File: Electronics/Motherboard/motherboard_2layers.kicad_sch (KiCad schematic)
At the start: 55 parts, among them J1 DX07S024JJ3R1300, J2 Conn_02x10_Odd_Even, M1 AO3400A, M2 AO3400A, M3 AO3400A, U1 AMS1117-3.3, U2 TMC2209_SILENTSTEPSTICK, U3 TMC2209_SILENTSTEPSTICK, U4 TMC2209_SILENTSTEPSTICK, U5 TMC2209_SILENTSTEPSTICK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

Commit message: yay finished
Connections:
- net DIAG_M3: now also U7.96 (PE2); no longer U7.2 (PC10)
- net DIR_M4: now also U7.76 (PC8); no longer U7.72 (PF8)
- net EN_BTN: now also U7.21 (PC0); no longer U7.44 (PE11)
- net EN_FOR: now also U7.23 (PC2); no longer U7.46 (PE13)
- net EN_M1: now also U7.78 (PD0); no longer U7.68 (PD15)
- net EN_REV: now also U7.22 (PC1); no longer U7.45 (PE12)
- net STEP_M1: now also U7.79 (PD1); no longer U7.67 (PD14)
- net STEP_M2: now also U7.97 (PE3); no longer U7.33 (PC4)
- net STEP_M3: now also U7.95 (PE1); no longer U7.3 (PC11)
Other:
- note added: "Voltage Reg 3.3v"
- note added: "Voltage Reg. 5v"
- note removed: "Voltage Regulator"
- moved on the sheet: C8, C9, U6

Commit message: updated some files
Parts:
- added U8: STM32F405RGTx, Package_QFP:LQFP-64_10x10mm_P0.5mm, symbol MCU_ST_STM32F4:STM32F405RGTx
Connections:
- net STEP_M2: now also U7.33 (PC4); no longer U7.97 (PE3)
- net STEP_M4: now also U7.97 (PE3); no longer U7.1 (PB9)
- new net: U8.18 (VSS), U8.63 (VSS)
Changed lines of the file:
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@@
 		(color 0 0 0 0)
 	)
+	(bus_entry
+		(at 103.124 97.028)
+		(size 2.54 2.54)
+		(stroke
+			(width 0)
+			(type default)
+		)
+	)
+	(bus_entry
+		(at 79.248 41.402)
+		(size 2.54 2.54)
+		(stroke
+			(width 0)
+			(type default)
+		)
+	)
 	(wire
 		(pts
@@
 		)
 	)
+	(global_label "STEP_M4"
+		(shape input)
+		(at 39.37 132.08 180)
+		(fields_autoplaced yes)
+		(effects
+			(font
+				(size 1.27 1.27)
+			)
+			(justify right)
+		)
+		(property "Intersheetrefs" "${INTERSHEET_REFS}"
+			(at 28.1602 132.08 0)
+			(effects
+				(font
+					(size 1.27 1.27)
+				)
+				(justify right)
+				(hide yes)
+			)
+		)
+	)
 	(global_label "ABL"
 		(shape input)
@@
 		)
 	)
-	(global_label "STEP_M4"
-		(shape input)
-		(at 85.09 147.32 0)
-		(fields_autoplaced yes)
-		(effects
-			(font
-				(size 1.27 1.27)
-			)
-			(justify left)
-		)
-		(property "Intersheetrefs" "${INTERSHEET_REFS}"
-			(at 96.2998 147.32 0)
-			(effects
-				(font
-					(size 1.27 1.27)
-				)
-				(justify left)
-				(hide yes)
-			)
-		)
-	)
 	(global_label "UART_TX"
 		(shape input)
@@
 		)
 	)
-	(global_label "STEP_M2"
-		(shape input)
-		(at 39.37 132.08 180)
-		(fields_autoplaced yes)
-		(effects
-			(font
-				(size 1.27 1.27)
-			)
-			(justify right)
-		)
-		(property "Intersheetrefs" "${INTERSHEET_REFS}"
-			(at 28.1602 132.08 0)
-			(effects
-				(font
-					(size 1.27 1.27)
-				)
-				(justify right)
-				(hide yes)
-			)
-		)
-	)
 	(global_label "EN_M3"
 		(shape input)
@@
 		)
 	)
+	(global_label "STEP_M2"
+		(shape input)
+		(at 85.09 177.8 0)
+		(fields_autoplaced yes)
+		(effects
+			(font
+				(size 1.27 1.27)
+			)
+			(justify left)
+		)
+		(property "Intersheetrefs" "${INTERSHEET_REFS}"
+			(at 96.2998 177.8 0)
+			(effects
+				(font
+					(size 1.27 1.27)
+				)
+				(justify left)
+				(hide yes)
+			)
+		)
+	)
 	(global_label "UART_TX"
 		(shape input)
@@
 					(unit 1)
 				)
+			)
+		)
+	)
+	(symbol
+		(lib_id "MCU_ST_STM32F4:STM32F405RGTx")
+		(at 119.888 122.428 0)
+		(unit 1)
+		(exclude_from_sim no)
+		(in_bom yes)
+		(on_board yes)
+		(dnp no)
+		(fields_autoplaced yes)
+		(property "Reference" "U8"
+			(at 124.6221 167.64 0)
+			(effects
+				(font
+					(size 1.27 1.27)
+				)
+				(justify left)
+			)
+		)
+		(property "Value" "STM32F405RGTx"
+			(at 124.6221 170.18 0)
+			(effects
+				(font
+					(size 1.27 1.27)
+				)
+				(justify left)
+			)
+		)
+		(property "Footprint" "Package_QFP:LQFP-64_10x10mm_P0.5mm"
+			(at 104.648 165.608 0)
+			(effects
+				(font
+					(size 1.27 1.27)
+				)
+				(justify right)
+				(hide yes)
+			)
+		)
+		(property "Datasheet" "https://www.st.com/resource/en/datasheet/stm32f405rg.pdf"
+			(at 119.888 122.428 0)
+			(effects
+				(font
+					(size 1.27 1.27)
+				)
+				(hide yes)
+			)
+		)
+		(property "Description" "STMicroelectronics Arm Cortex-M4 MCU, 1024KB flash, 192KB RAM, 168 MHz, 1.8-3.6V, 51 GPIO, LQFP64"
+			(at 119.888 122.428 0)
+			(effects
+				(font
+					(size 1.27 1.27)
+				)
+				(hide yes)
+			)
+		)
+		(pin "63"
+		)
+		(pin "7"
+		)
+		(pin "50"
+		)
+		(pin "31"
+		)
+		(pin "33"
+		)
+		(pin "12"
+		)
+		(pin "34"
+		)
+		(pin "39"
+		)
+		(pin "44"
+		)
+		(pin "46"
+		)
+		(pin "60"
+		)
+		(pin "20"
+		)
+		(pin "36"
+		)
+		(pin "55"
+		)
+		(pin "15"
+		)
+		(pin "18"
+		)
+		(pin "37"
+		)
+		(pin "58"
+		)
+		(pin "2"
+		)
+		(pin "47"
+		)
+		(pin "5"
+		)
+		(pin "54"
+		)
+		(pin "62"
+		)
+		(pin "13"
+		)
+		(pin "53"
+		)
+		(pin "56"
+		)
+		(pin "27"
+		)
+		(pin "42"
+		)
+		(pin "59"
+		)
+		(pin "40"
+		)
+		(pin "64"
+		)
+		(pin "19"
+		)
+		(pin "48"
+		)
+		(pin "23"
+		)
+		(pin "32"
+		)
+		(pin "22"
+		)
+		(pin "41"
+		)
+		(pin "17"
+		)
+		(pin "49"
+		)
+		(pin "30"
+		)
+		(pin "10"
+		)
+		(pin "51"
+		)
+		(pin "43"
+		)
+		(pin "57"
+		)
+		(pin "6"
+		)
+		(pin "61"
+		)
+		(pin "26"
+		)
+		(pin "1"
+		)
+		(pin "11"
+		)
+		(pin "14"
+		)
+		(pin "16"
+		)
+		(pin "21"
+		)
+		(pin "25"
+		)
+		(pin "28"
+		)
+		(pin "29"
+		)
+		(pin "3"
+		)
+		(pin "38"
+		)
+		(pin "4"
+		)
+		(pin "45"
+		)
+		(pin "52"
+		)
+		(pin "35"
+		)
+		(pin "24"
+		)
+		(pin "9"
+		)
+		(pin "8"
+		)
+		(instances
+			(project ""
+				(path "/9290e430-09f5-4a3f-8744-4071dceedc2e"
+					(reference "U8")
+					(unit 1)
+				)

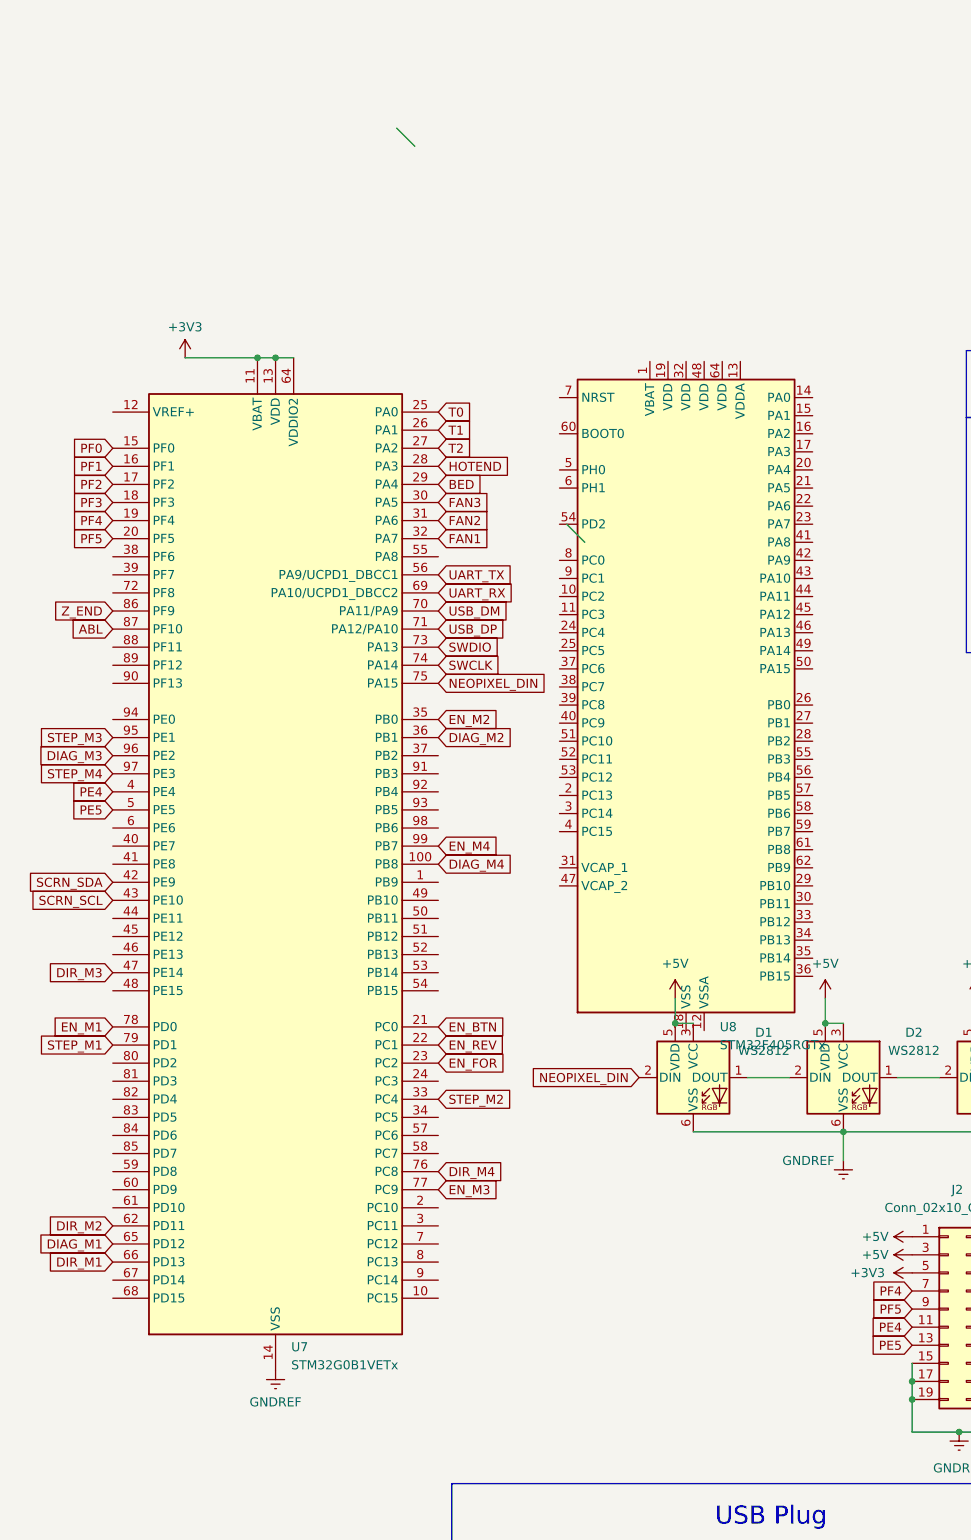
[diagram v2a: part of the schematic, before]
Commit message: updating the sch to work ebtter with the new mcu
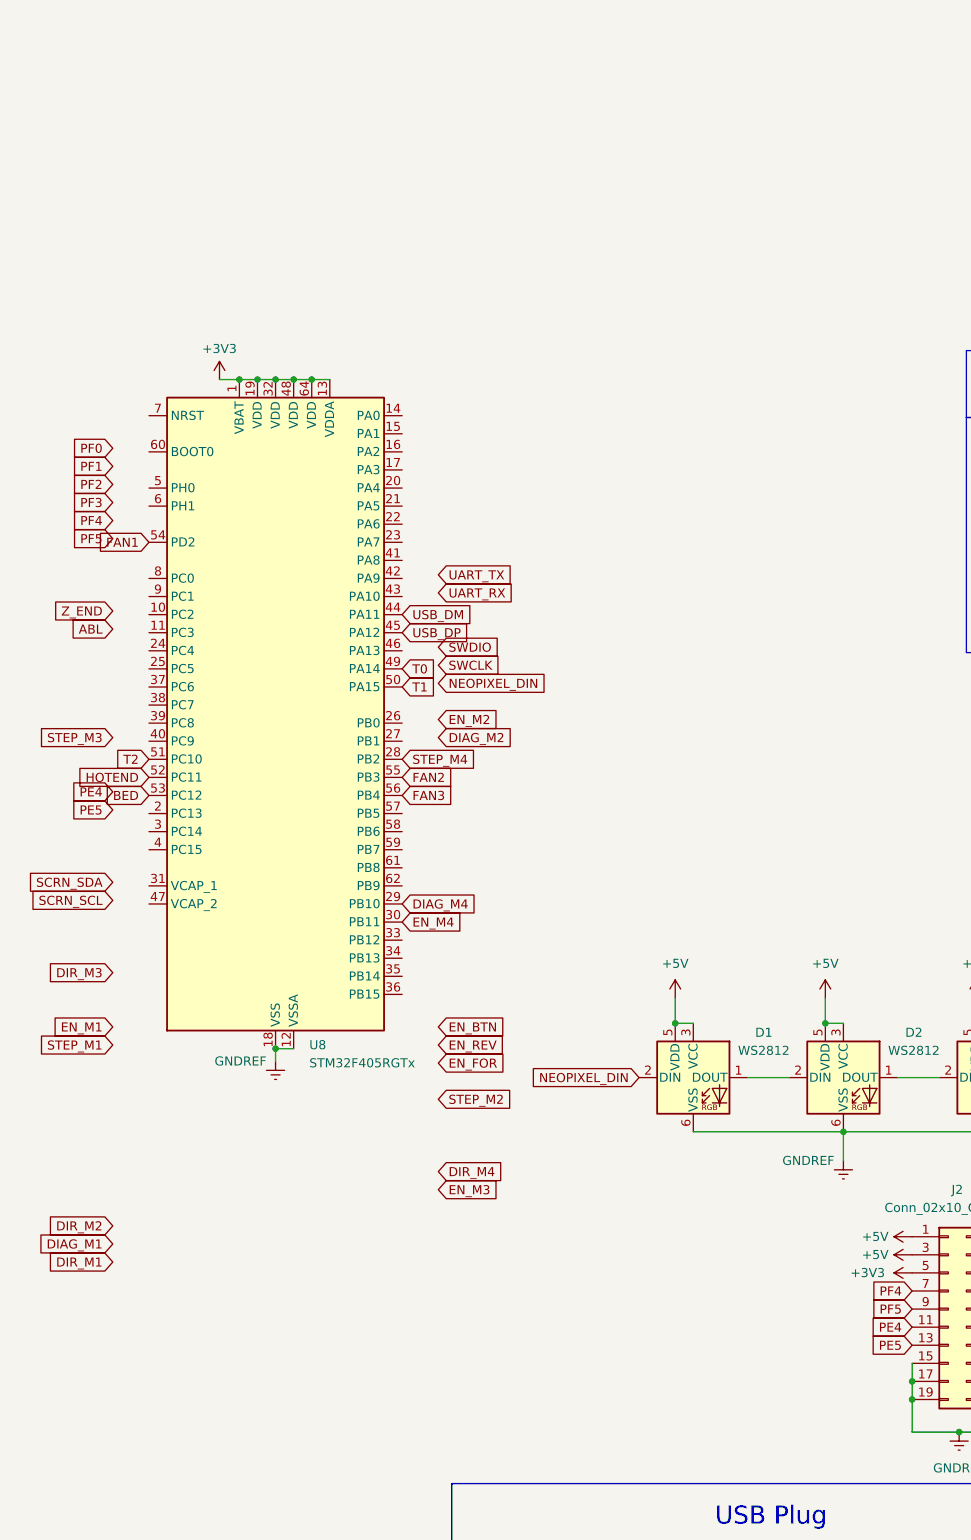
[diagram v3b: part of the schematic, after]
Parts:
- removed U7: STM32G0B1VETx, Package_QFP:LQFP-100_14x14mm_P0.5mm, symbol MCU_ST_STM32G0:STM32G0B1VETx
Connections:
- net +3V3: now also U8.1 (VBAT), U8.13 (VDDA), U8.19 (VDD), U8.32 (VDD), U8.48 (VDD), U8.64 (VDD)
- net BED: now also U8.53 (PC12)
- net DIAG_M4: now also U8.29 (PB10)
- net EN_M4: now also U8.30 (PB11)
- net FAN1: now also U8.54 (PD2)
- net FAN2: now also U8.55 (PB3)
- net FAN3: now also U8.56 (PB4)
- net GNDREF: now also U8.12 (VSSA), U8.18 (VSS), U8.63 (VSS)
- net HOTEND: now also U8.52 (PC11)
- net STEP_M4: now also U8.28 (PB2)
- net T0: now also U8.49 (PA14)
- net T1: now also U8.50 (PA15)
- net T2: now also U8.51 (PC10)
- net USB_DM: now also U8.44 (PA11)
- net USB_DP: now also U8.45 (PA12)
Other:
- moved on the sheet: U8

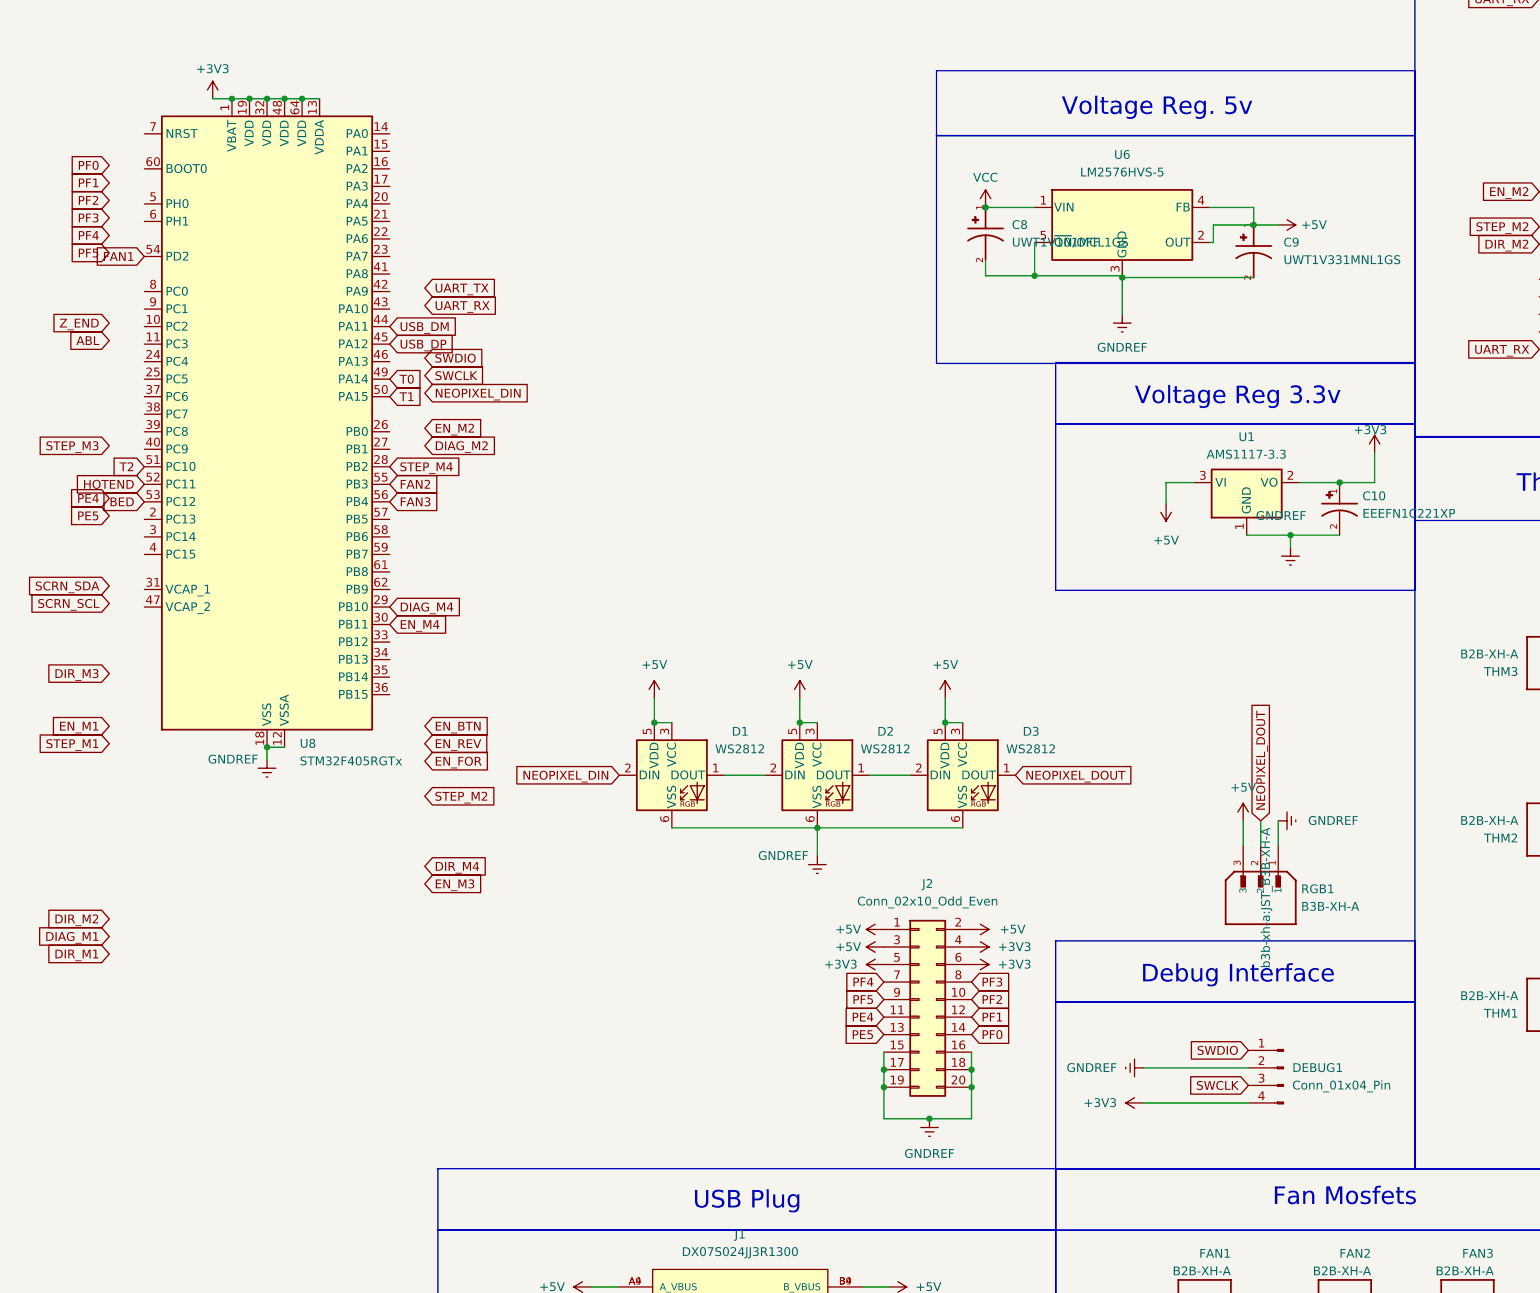
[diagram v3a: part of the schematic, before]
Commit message: basically finished schematic, tiny bit more needs to be done
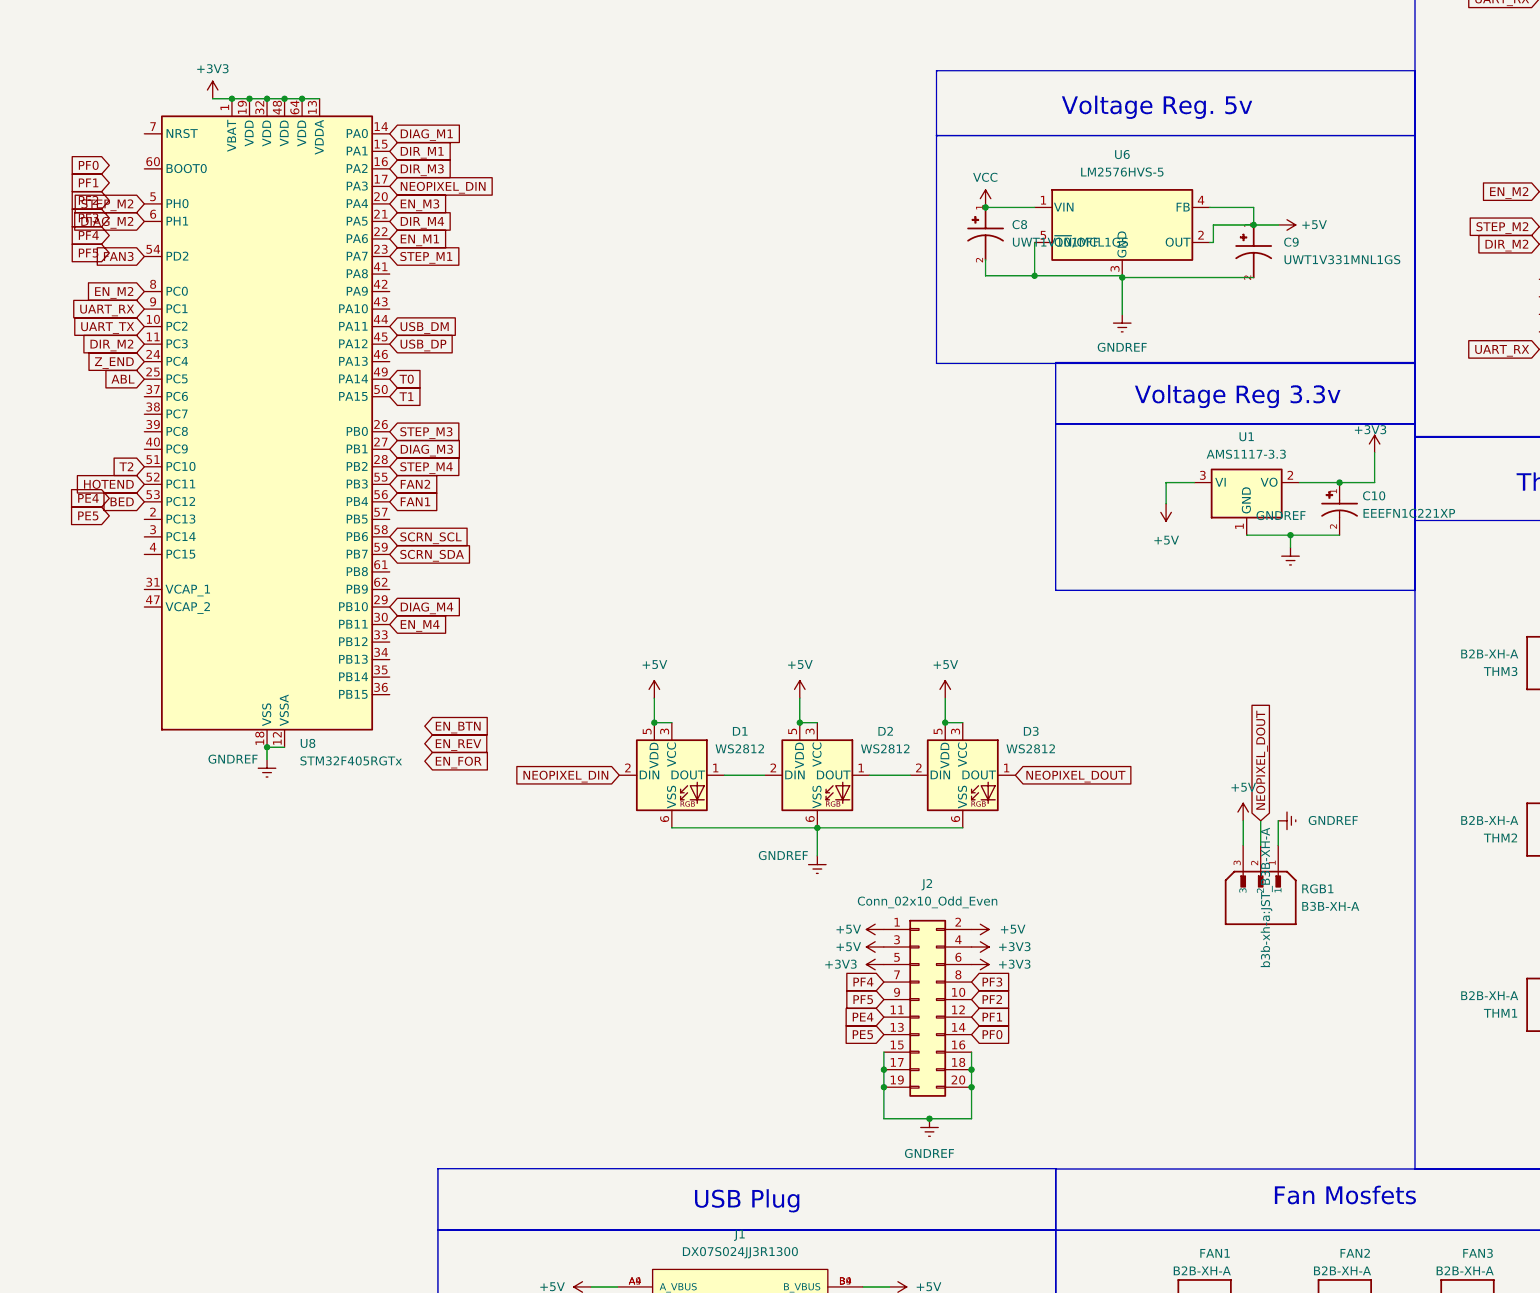
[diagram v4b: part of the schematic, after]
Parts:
- removed DEBUG1: Conn_01x04_Pin, PinHeader:PinHeader_1x04_P2.54mm_Vertical, symbol Connector:Conn_01x04_Pin
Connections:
- net ABL: now also U8.25 (PC5)
- net DIAG_M1: now also U8.14 (PA0)
- net DIAG_M2: now also U8.6 (PH1)
- net DIAG_M3: now also U8.27 (PB1)
- net DIR_M1: now also U8.15 (PA1)
- net DIR_M2: now also U8.11 (PC3)
- net DIR_M3: now also U8.16 (PA2)
- net DIR_M4: now also U8.21 (PA5)
- net EN_M1: now also U8.22 (PA6)
- net EN_M2: now also U8.8 (PC0)
- net EN_M3: now also U8.20 (PA4)
- net FAN1: now also U8.56 (PB4); no longer U8.54 (PD2)
- net FAN3: now also U8.54 (PD2); no longer U8.56 (PB4)
- net NEOPIXEL_DIN: now also U8.17 (PA3)
- net SCRN_SCL: now also U8.58 (PB6)
- net SCRN_SDA: now also U8.59 (PB7)
- net STEP_M1: now also U8.23 (PA7)
- net STEP_M2: now also U8.5 (PH0)
- net STEP_M3: now also U8.26 (PB0)
- net UART_RX: now also U8.9 (PC1)
- net UART_TX: now also U8.10 (PC2)
- net Z_END: now also U8.24 (PC4)
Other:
- note removed: "Debug Interface"

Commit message: tiny bit of routing, more needs to be done
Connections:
- net PE4 is gone; now on net PC8: J2.11 (Pin_11)
- net PE5 is gone; now on net PC9: J2.13 (Pin_13)
- net PF0 is gone; now on net PC6: J2.14 (Pin_14)
- net PF1 is gone; now on net PC7: J2.12 (Pin_12)
- net PF2 is gone; now on net PB14: J2.10 (Pin_10)
- net PF3 is gone; now on net PB12: J2.8 (Pin_8)
- net PF4 is gone; now on net PB13: J2.7 (Pin_7)
- net PF5 is gone; now on net PB15: J2.9 (Pin_9)
- net EN_BTN: now also U8.43 (PA10)
- net EN_FOR: now also U8.41 (PA8)
- net EN_REV: now also U8.42 (PA9)
- net PB12: now reaches U8.33 (PB12)
- net PB13: now reaches U8.34 (PB13)
- net PB14: now reaches U8.35 (PB14)
- net PB15: now reaches U8.36 (PB15)
- net PC6: now reaches U8.37 (PC6)
- net PC7: now reaches U8.38 (PC7)
- net PC8: now reaches U8.39 (PC8)
- net PC9: now reaches U8.40 (PC9)
